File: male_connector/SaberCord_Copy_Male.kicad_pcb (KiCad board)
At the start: 2 copper layers, 40.6 x 22.2 mm, 6 parts, among them J1 Conn_02x07_Row_Letter_Last, J2 Conn_02x12_Row_Letter_Last

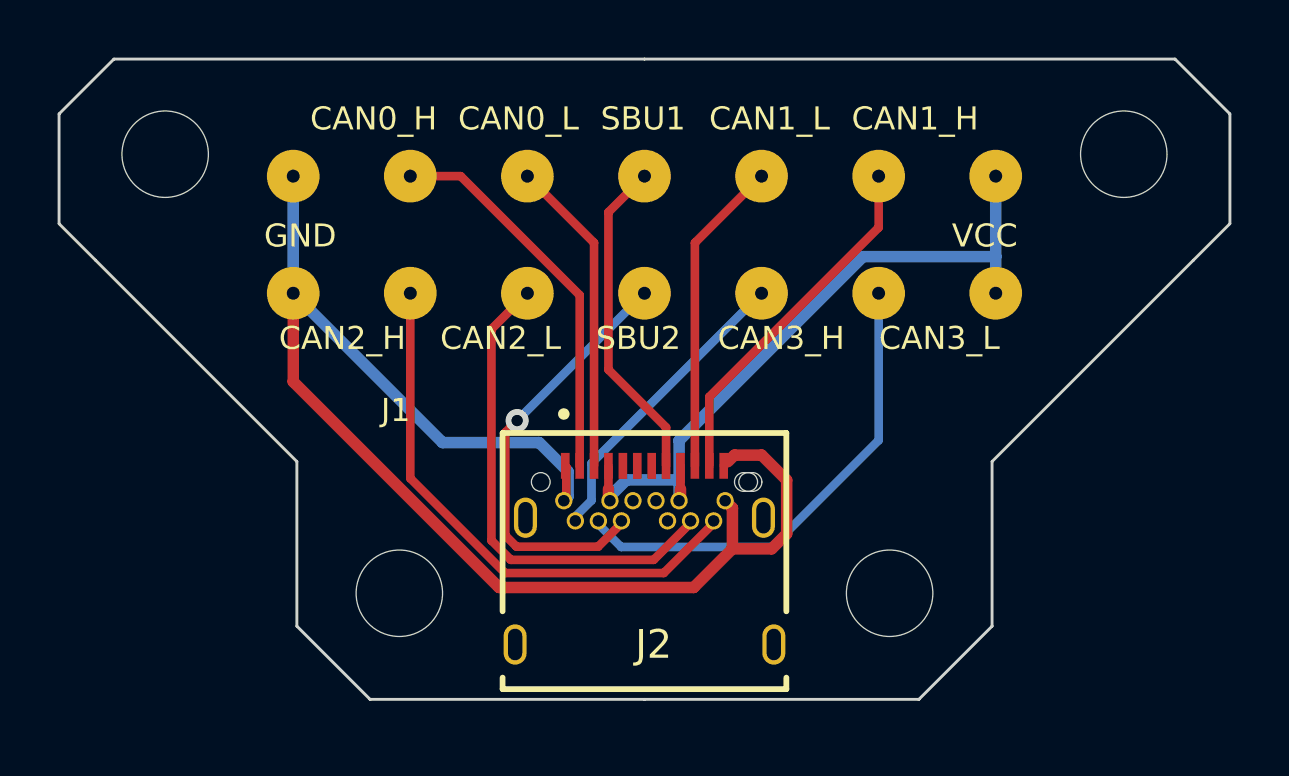
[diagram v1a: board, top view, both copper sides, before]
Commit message: change usb c connector export to jlcpcb
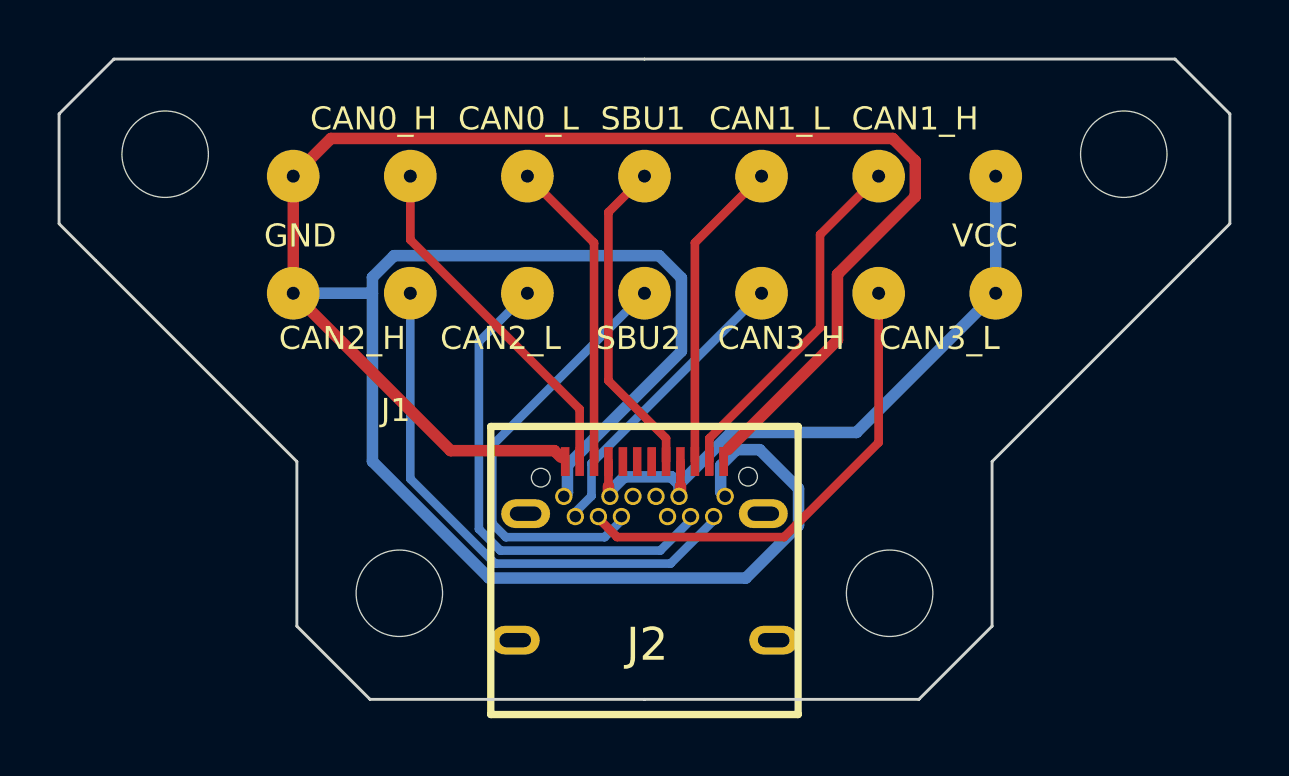
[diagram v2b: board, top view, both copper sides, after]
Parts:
- J2: footprint CommaPogo_Library:GCT_USB4056-03-A_REVA2 -> CommaPogo_Library:USB-C-SMD_HC005-1A1H1A103-0HR
- moved J2 3.25 mm to (140.3, 90.7)
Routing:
- net GND: track 48.8 -> 104.5 mm
- net +12V: track 25.0 -> 23.6 mm
- net /CAN0_H: track 13.5 -> 12.3 mm
- net /SBU2: track 15.0 -> 15.2 mm, vias 1 -> 0
